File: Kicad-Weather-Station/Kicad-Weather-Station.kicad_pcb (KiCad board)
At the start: 2 copper layers, 100 x 50 mm, 72 parts, among them CON1 Solar Panel, J1 MicroSD, P1 CONN_01X25, P2 CONN_01X25, P3 Rain Gauge, P4 Temperature/Humidity, P5 Wind Speed, P6 Air Pressure, P7 Battery, Q1 MMBT3904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

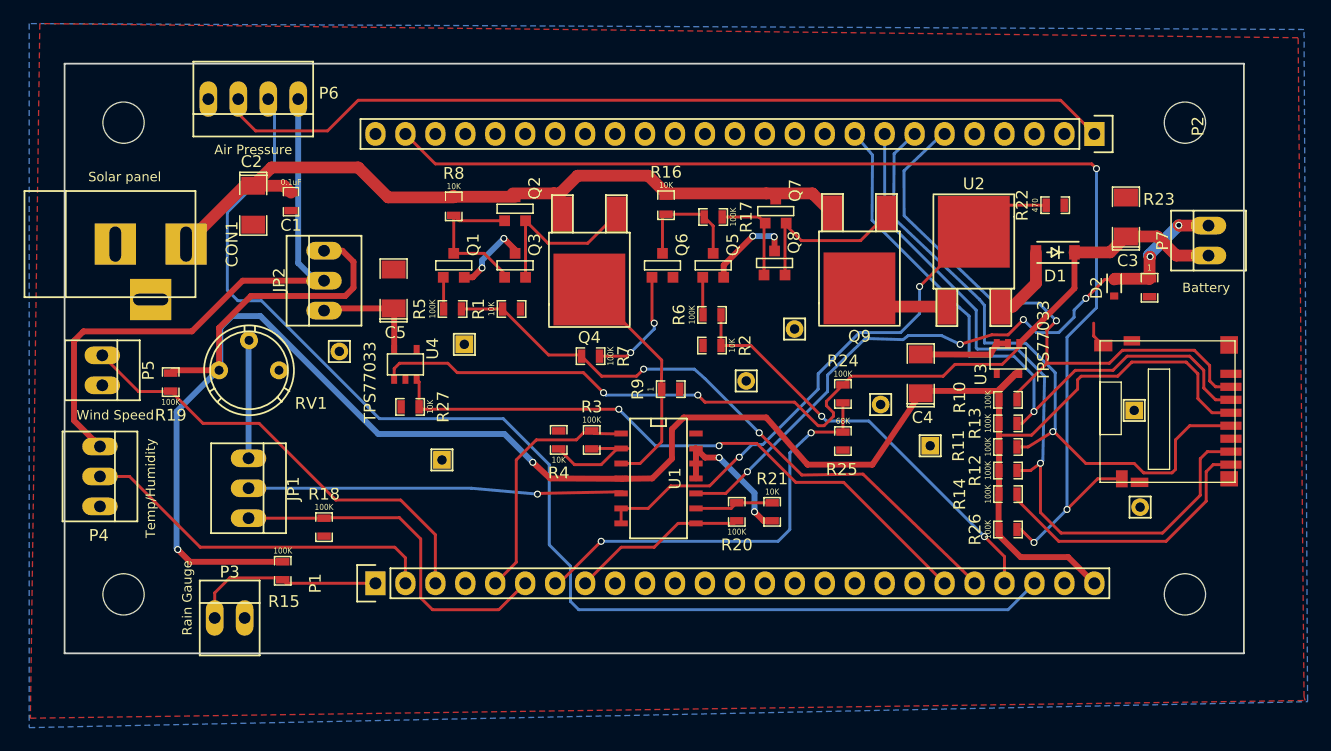
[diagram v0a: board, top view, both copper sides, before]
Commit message: Added missing inversion stage for battery charge MOSFET driver section. Removed clunky earth pin holes and added tracks with vias in the earthing part to ensure that all earths can be connected after zone fill.
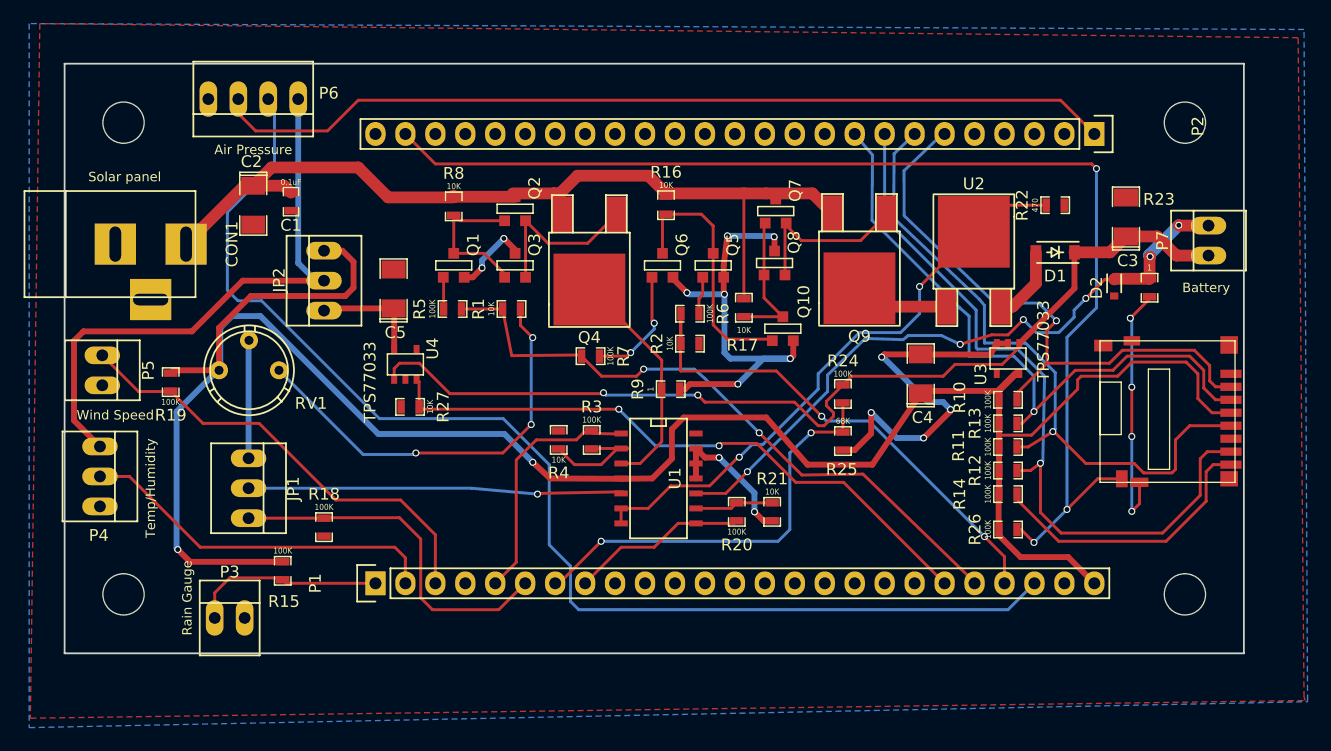
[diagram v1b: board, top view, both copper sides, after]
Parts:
- removed the ? at (92.0, 88.6)
- removed the ? at (133.4, 87.4)
- removed the ? at (93.9, 78.8)
- removed the ? at (150.7, 84.4)
- removed the ? at (121.9, 77.5)
- removed the ? at (117.8, 81.9)
- removed the ? at (83.3, 79.4)
- removed the ? at (129.2, 83.9)
- removed the ? at (151.2, 92.6)
- added Q10: MMBT3904, WeatherStation:SOT23EBC, F.Cu at (120.9, 77.5)
- R17: value 100K -> 10K
- moved R17 8.12 mm to (117.6, 75.7), turned to 270 degrees
- moved R2 1.88 mm to (113.0, 78.7), turned to 0 degrees
- moved R6 1.87 mm to (113.0, 76.2), turned to 180 degrees
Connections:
- Q5 pad 3: Net-(Q5-Pad3) -> Net-(Q10-Pad2)
- Q6 pad 3: Net-(Q5-Pad3) -> Net-(Q10-Pad2)
- Q7 pad 2: Net-(Q7-Pad2) -> Net-(Q10-Pad3)
- Q8 pad 2: Net-(Q7-Pad2) -> Net-(Q10-Pad3)
- R16 pad 2: Net-(Q5-Pad3) -> Net-(Q10-Pad2)
- R17 pad 1: Net-(Q7-Pad2) -> Net-(C1-Pad1)
- R17 pad 2: Net-(Q5-Pad3) -> Net-(Q10-Pad3)
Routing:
- net Earth: track 37.0 -> 147.1 mm, vias 6 -> 21
- net Net-(Q10-Pad2): track 0.00 -> 21.8 mm
- net Net-(Q10-Pad3): track 0.00 -> 12.0 mm
- net Net-(Q5-Pad3): track 10.2 -> 0.00 mm
- net Net-(C1-Pad1): track 67.3 -> 76.8 mm
- net Net-(Q7-Pad2): track 8.22 -> 0.00 mm
- net PB5: track 36.3 -> 43.7 mm
- net PB4: track 53.6 -> 55.2 mm
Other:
- board text added: "Weather Station Rev 1.1 K. Sarkies 07/02/2018 license cc-by-sa www.jiggerjuice.info"

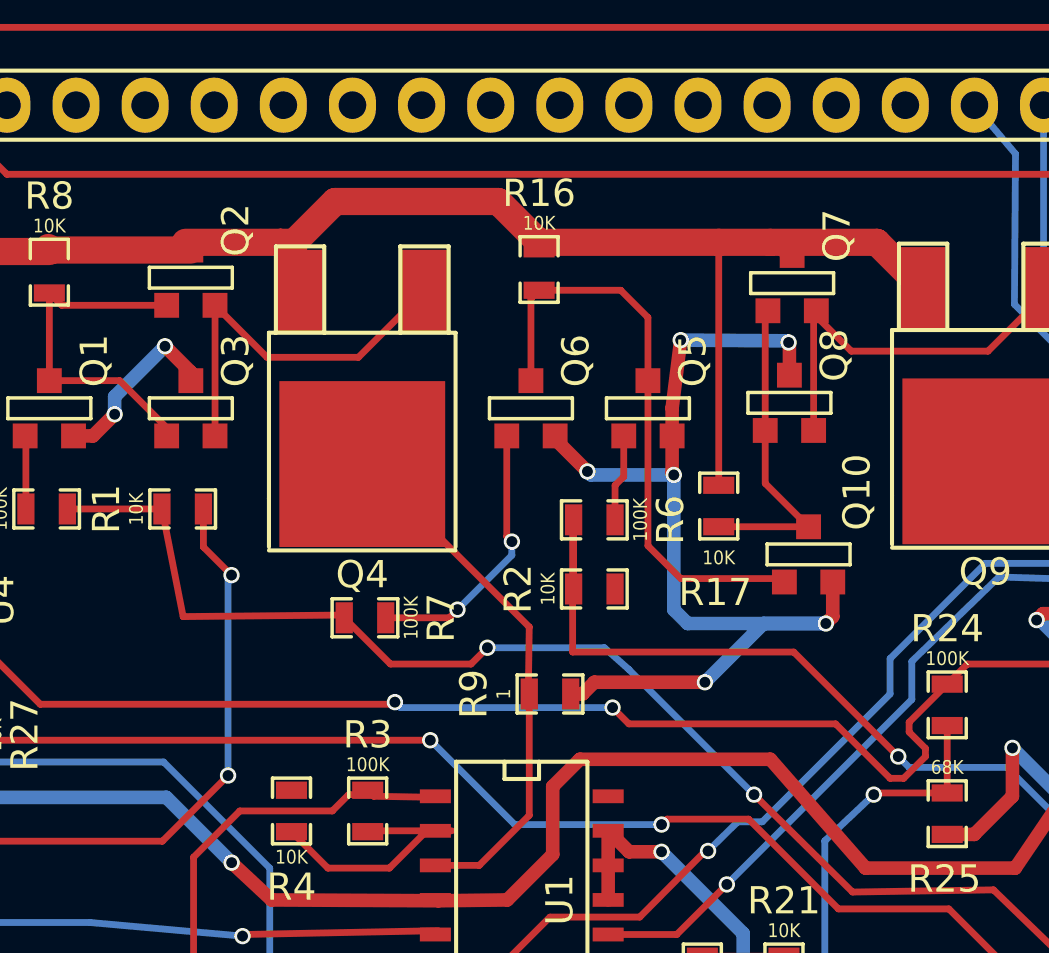
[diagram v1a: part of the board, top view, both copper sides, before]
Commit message: Second version of changes to fix MOSFET drivers. Use AND gate form of inverter to ensure that battery charge MOSFET is off when solar panel measurement is on. This does not need any transistors and is two resistors less.
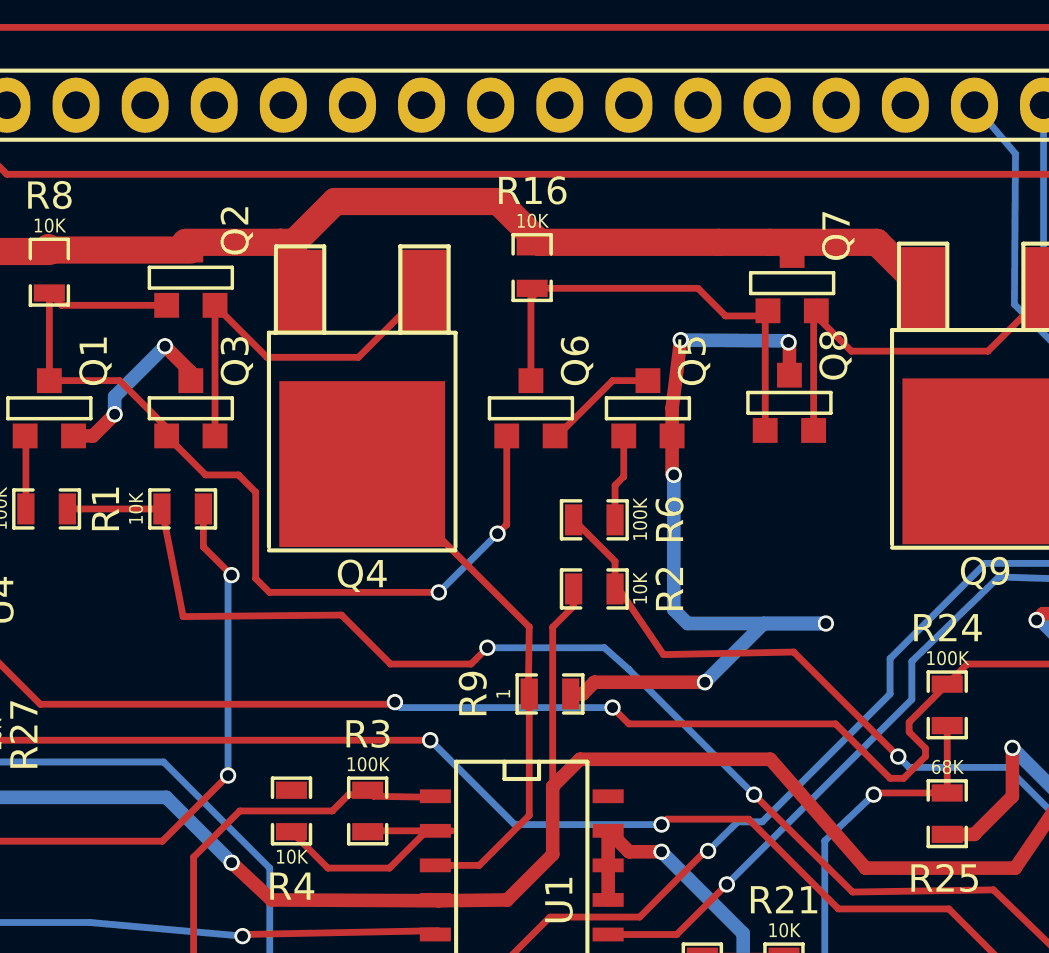
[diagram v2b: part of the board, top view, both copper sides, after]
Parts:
- removed Q10: MMBT3904, WeatherStation:SOT23EBC
- removed R17: 10K, WeatherStation:SM0603_Resistor
- removed R7: 100K, WeatherStation:SM0603_Resistor
- moved R16 0.27 mm to (110.7, 66.9)
- turned R2 to 180 degrees
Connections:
- Q5 pad 3: Net-(Q10-Pad2) -> Net-(Q5-Pad3)
- Q6 pad 1: Earth -> Net-(Q5-Pad3)
- Q6 pad 2: Net-(Q6-Pad2) -> Net-(Q1-Pad3)
- Q6 pad 3: Net-(Q10-Pad2) -> Net-(Q6-Pad3)
- Q7 pad 2: Net-(Q10-Pad3) -> Net-(Q6-Pad3)
- Q8 pad 2: Net-(Q10-Pad3) -> Net-(Q6-Pad3)
- R16 pad 2: Net-(Q10-Pad2) -> Net-(Q6-Pad3)
- R2 pad 2: Earth -> +3.3V-M
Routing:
- net Net-(Q10-Pad2): track 21.8 -> 0.00 mm
- net Net-(Q1-Pad3): track 13.1 -> 34.1 mm, vias 0 -> 2
- net Net-(Q6-Pad3): track 0.00 -> 17.1 mm
- net Net-(Q10-Pad3): track 12.0 -> 0.00 mm
- net Net-(Q6-Pad2): track 10.1 -> 0.00 mm, vias 2 -> 0
- net Net-(C1-Pad1): track 76.8 -> 67.9 mm
- net +3.3V-M: track 190.7 -> 198.2 mm
- net Earth: track 147.1 -> 140.5 mm, vias 21 -> 20
- net Net-(Q5-Pad3): track 0.00 -> 4.37 mm
- net PB5: track 43.7 -> 39.5 mm
